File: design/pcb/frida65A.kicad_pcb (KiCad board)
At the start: 4 copper layers, 100 x 100 mm, 105 parts, among them J1 DisplayPort Molex 472720024, J10 VIN CFG, J11 TP AMP, J12 MiniFitJr Molex 469990014, J13 POWER, J14 RJ45 Molex 446200002, J15 SPI TP, J2 TP CLOCKS, J3 SMA Molex 733910070, J4 SMA Molex 733910070, J5 DIFF/SE CFG, J6 TERM CFG, J7 ATTEN CFG, J8 SMA Molex 733910070, J9 TERM CFG, Q1 Q_PMOS_DGS, U1 DiffAmp TI THS4541, U2 TI LevelShifter SN74AXC8T245R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, U3 ASIC FRIDA 65A

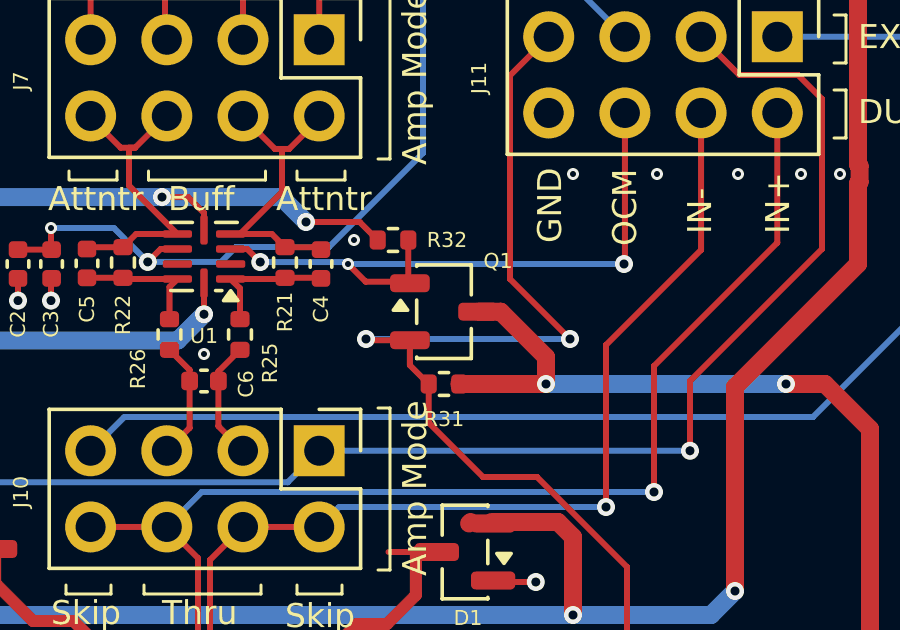
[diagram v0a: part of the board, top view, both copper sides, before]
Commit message: fix(pcb): correct Q1 pin mapping
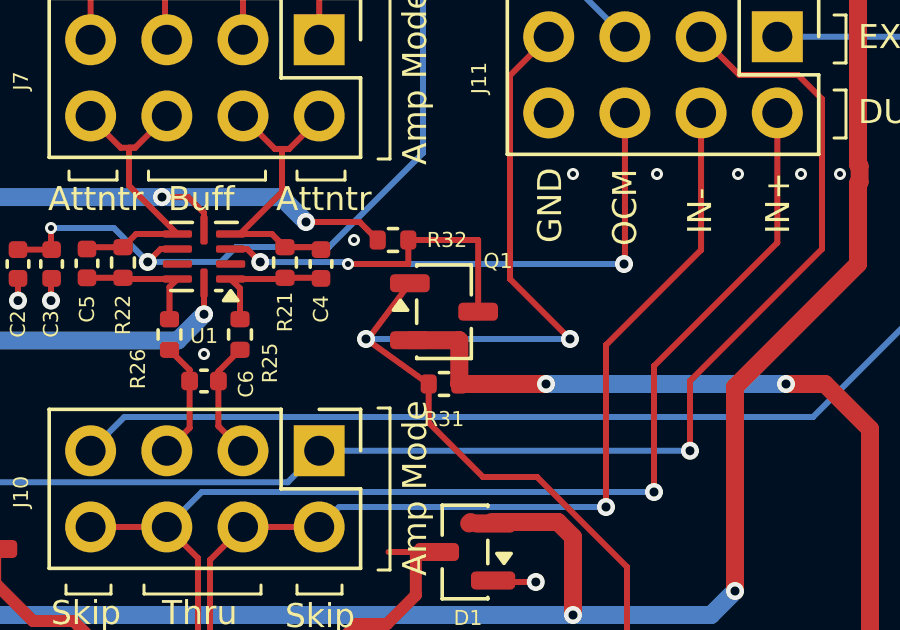
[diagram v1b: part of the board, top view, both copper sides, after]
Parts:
- Q1: value Q_PMOS_DGS -> Q_PMOS_GSD
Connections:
- Q1 pad 1: /AMP_PD_N -> /AMP_PD_EXT
- Q1 pad 2: /AMP_PD_EXT -> /VDD_BDAQ
- Q1 pad 3: /VDD_BDAQ -> /AMP_PD_N
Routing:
- net /AMP_PD_N: track 22.2 -> 25.9 mm
- net /AMP_PD_EXT: track 84.7 -> 86.5 mm
- net /VDD_BDAQ: track 112.2 -> 111.4 mm
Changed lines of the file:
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@@
 			)
 		)
-		(property "Value" "Q_PMOS_DGS"
+		(property "Value" "Q_PMOS_GSD"
 			(at 0 2.4 0)
 			(layer "F.Fab")
@@
 			)
 		)
-		(property "Description" "P-MOSFET transistor, drain/gate/source"
+		(property "Description" "P-MOSFET transistor, gate/source/drain"
 			(at 0 0 0)
 			(layer "F.Fab")
@@
 			(layers "F.Cu" "F.Mask" "F.Paste")
 			(roundrect_rratio 0.25)
-			(net 60 "/AMP_PD_N")
-			(pinfunction "D")
-			(pintype "passive")
+			(net 59 "/AMP_PD_EXT")
+			(pinfunction "G")
+			(pintype "input")
 		)
 		(pad "2" smd roundrect
@@
 			(layers "F.Cu" "F.Mask" "F.Paste")
 			(roundrect_rratio 0.25)
-			(net 59 "/AMP_PD_EXT")
-			(pinfunction "G")
-			(pintype "input")
+			(net 58 "/VDD_BDAQ")
+			(pinfunction "S")
+			(pintype "passive")
 		)
 		(pad "3" smd roundrect
@@
 			(layers "F.Cu" "F.Mask" "F.Paste")
 			(roundrect_rratio 0.25)
-			(net 58 "/VDD_BDAQ")
-			(pinfunction "S")
+			(net 60 "/AMP_PD_N")
+			(pinfunction "D")
 			(pintype "passive")
 		)
@@
 	)
 	(segment
-		(start 159.3375 81.79)
-		(end 159.4 81.8525)
-		(width 0.2)
-		(layer "F.Cu")
-		(net 58)
-	)
-	(segment
 		(start 173.790003 126.699997)
 		(end 173 127.49)
@@
 	)
 	(segment
-		(start 160.09 81.79)
-		(end 159.3375 81.79)
+		(start 157.0625 82.74)
+		(end 158.71 82.74)
+		(width 0.6)
+		(layer "F.Cu")
+		(net 58)
+	)
+	(segment
+		(start 158.71 82.74)
+		(end 158.71 84.2)
 		(width 0.6)
 		(layer "F.Cu")
@@
 	)
 	(segment
-		(start 161.6 84.2)
-		(end 161.6 83.3)
-		(width 0.6)
-		(layer "F.Cu")
-		(net 58)
-	)
-	(segment
-		(start 161.6 83.3)
-		(end 160.09 81.79)
-		(width 0.6)
-		(layer "F.Cu")
-		(net 58)
-	)
-	(segment
 		(start 170.38 130.4)
 		(end 171.388 130.4)
@@
 	)
 	(segment
-		(start 157.0625 82.74)
+		(start 157.0625 80.84)
 		(end 155.64 82.74)
 		(width 0.2)
@@
 	)
 	(segment
-		(start 157.0625 83.5725)
+		(start 155.6 82.7)
 		(end 157.69 84.2)
 		(width 0.2)
@@
 		(net 59)
 	)
-	(segment
-		(start 157.0625 82.74)
-		(end 157.0625 83.5725)
-		(width 0.2)
-		(layer "F.Cu")
-		(net 59)
-	)
 	(via
 		(at 155.6 82.7)
@@
 	)
 	(segment
-		(start 155.59 80.79)
-		(end 155 80.2)
+		(start 159.3375 81.79)
+		(end 159.3375 79.4)
 		(width 0.2)
 		(layer "F.Cu")
@@
 	)
 	(segment
-		(start 157.01 80.7875)
-		(end 157.0625 80.84)
+		(start 159.3375 79.4)
+		(end 157.01 79.4)
 		(width 0.2)
 		(layer "F.Cu")
@@
 	)
 	(segment
-		(start 157.0625 80.84)
-		(end 157.0125 80.79)
-		(width 0.2)
-		(layer "F.Cu")
-		(net 60)
-	)
-	(segment
-		(start 157.0125 80.79)
-		(end 155.59 80.79)
+		(start 157.01 79.4)
+		(end 157.01 80.2)
 		(width 0.2)
 		(layer "F.Cu")
@@
 	)
 	(segment
-		(start 157.01 79.4)
-		(end 157.01 80.7875)
+		(start 157.01 80.2)
+		(end 155 80.2)
 		(width 0.2)
 		(layer "F.Cu")
